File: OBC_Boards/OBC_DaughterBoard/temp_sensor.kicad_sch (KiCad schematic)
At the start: 5 parts, among them U1 MCP9808T-E{slash}MC

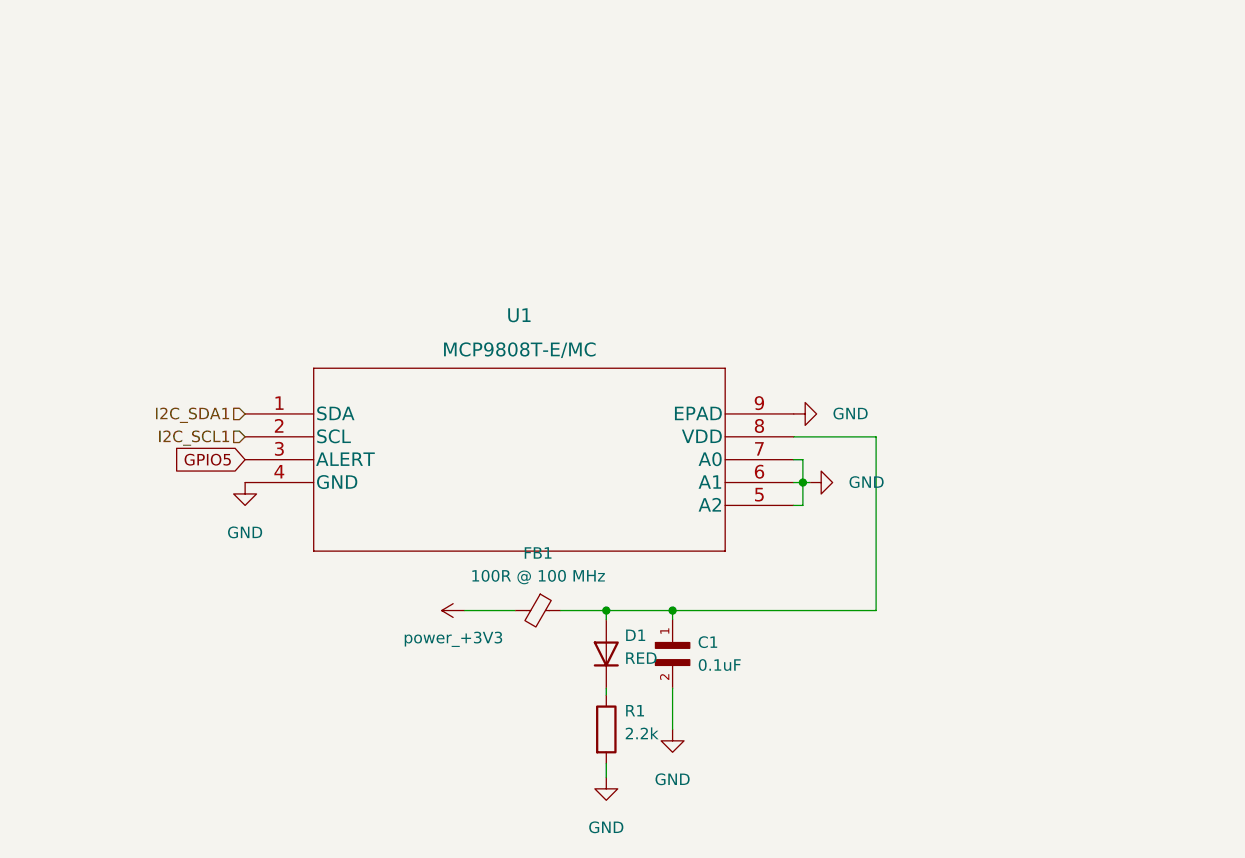
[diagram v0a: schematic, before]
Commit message: obc: daughterboard: clean up all schematics for easier reworks
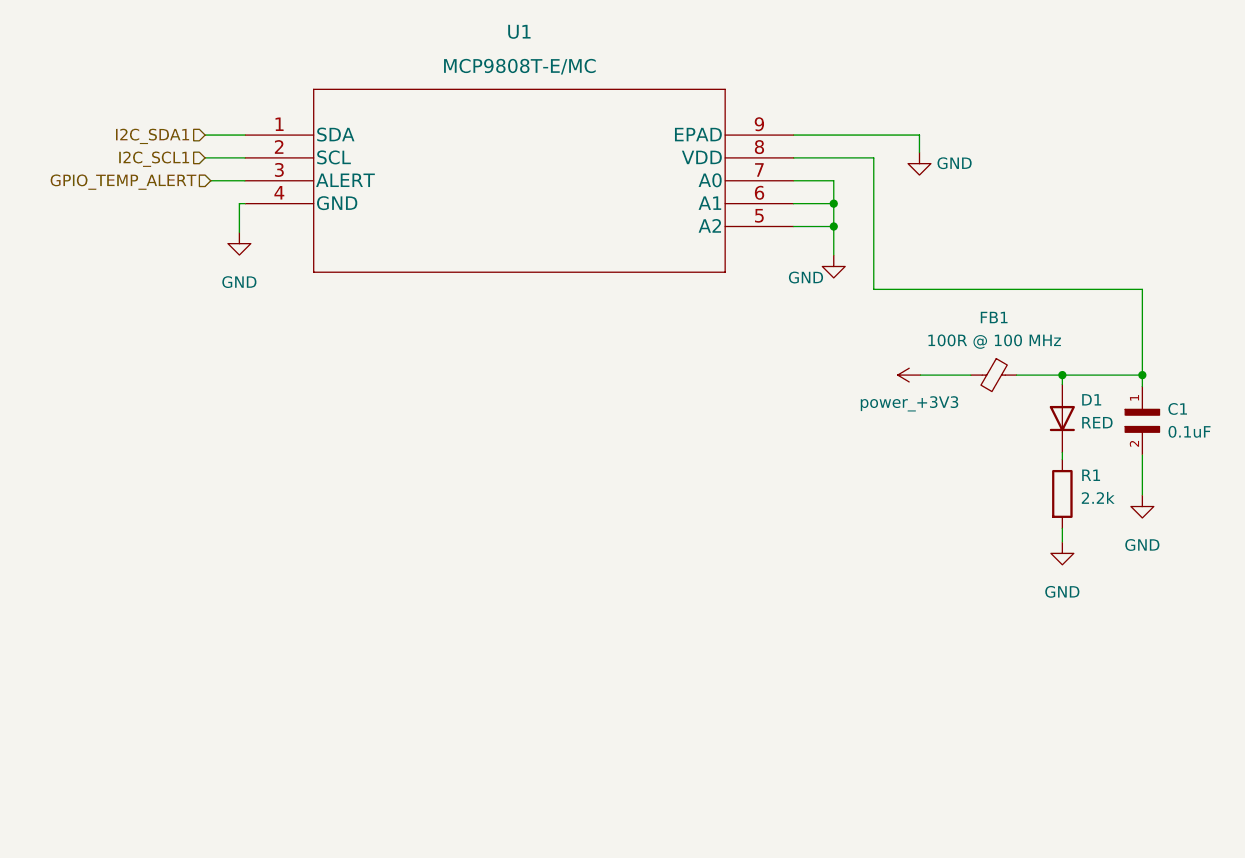
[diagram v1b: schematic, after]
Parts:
- U1: footprint Daughterboard_footprints:SOP65P490X110-8N -> DFN8_2x3MC_MCH
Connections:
- net GPIO5 renamed GPIO_TEMP_ALERT
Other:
- moved on the sheet: C1, D1, FB1, R1

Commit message: footprint fix
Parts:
- U1: footprint DFN8_2x3MC_MCH -> Daughterboard_footprints:MCP9808T-E&slash_MC
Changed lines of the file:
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@@
       (effects (font (size 1.524 1.524)))
     )
-    (property "Footprint" "DFN8_2x3MC_MCH" (id 2) (at 151.13 35.814 0)
+    (property "Footprint" "Daughterboard_footprints:MCP9808T-E&slash_MC" (id 2) (at 151.13 35.814 0)
       (effects (font (size 1.524 1.524)) hide)
     )
